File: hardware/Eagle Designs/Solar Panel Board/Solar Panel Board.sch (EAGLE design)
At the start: 34 parts, among them J1 MOLEX_503763-0291MOLEX_503763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, J2 MOLEX_503763-0491MOLEX_503763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

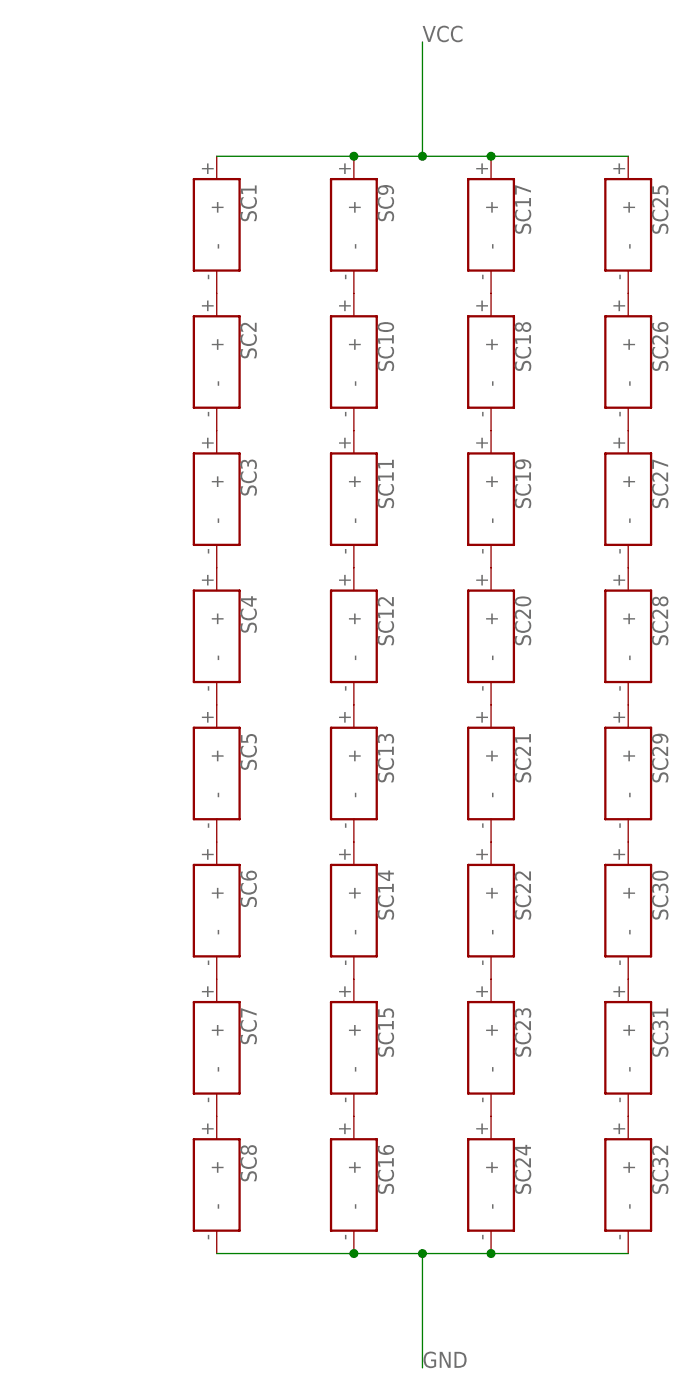
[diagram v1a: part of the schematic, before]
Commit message: Updated solar panel boards
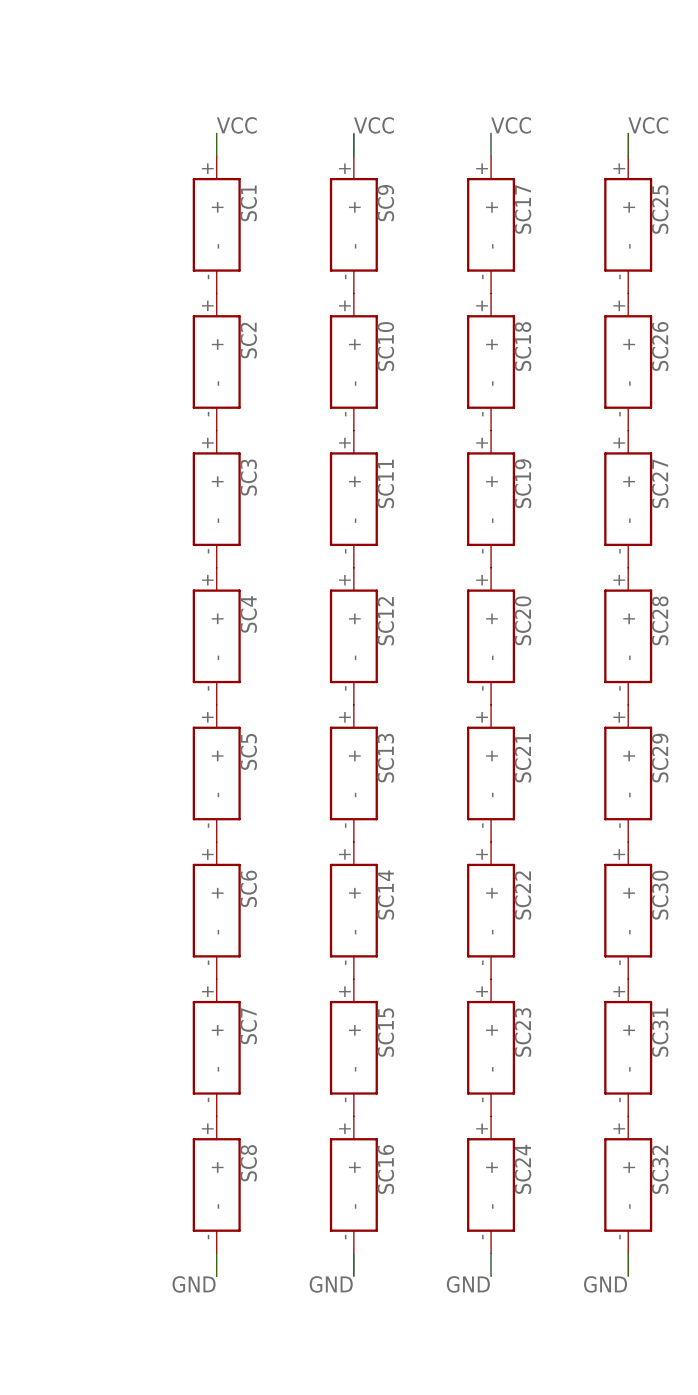
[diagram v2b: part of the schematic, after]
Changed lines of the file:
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@@
 </segment>
 <segment>
-<pinref part="J2" gate="G$0" pin="1"/>
+<pinref part="SC1" gate="G$1" pin="+"/>
+<wire x1="457.2" y1="43.18" x2="457.2" y2="45.72" width="0.1524" layer="91"/>
+<label x="457.2" y="45.72" size="1.778" layer="95"/>
+</segment>
+<segment>
+<pinref part="SC9" gate="G$1" pin="+"/>
+<wire x1="472.44" y1="43.18" x2="472.44" y2="45.72" width="0.1524" layer="91"/>
+<label x="472.44" y="45.72" size="1.778" layer="95"/>
+</segment>
+<segment>
+<pinref part="SC17" gate="G$1" pin="+"/>
+<wire x1="487.68" y1="43.18" x2="487.68" y2="45.72" width="0.1524" layer="91"/>
+<label x="487.68" y="45.72" size="1.778" layer="95"/>
+</segment>
+<segment>
+<pinref part="SC25" gate="G$1" pin="+"/>
+<wire x1="502.92" y1="43.18" x2="502.92" y2="45.72" width="0.1524" layer="91"/>
+<label x="502.92" y="45.72" size="1.778" layer="95"/>
+</segment>
+<segment>
 <wire x1="416.56" y1="-33.02" x2="419.1" y2="-33.02" width="0.1524" layer="91"/>
 <label x="419.1" y="-33.02" size="1.778" layer="95"/>
-</segment>
-<segment>
-<pinref part="SC25" gate="G$1" pin="+"/>
-<pinref part="SC17" gate="G$1" pin="+"/>
-<wire x1="487.68" y1="43.18" x2="502.92" y2="43.18" width="0.1524" layer="91"/>
-<junction x="487.68" y="43.18"/>
-<wire x1="480.06" y1="43.18" x2="487.68" y2="43.18" width="0.1524" layer="91"/>
-<wire x1="480.06" y1="43.18" x2="480.06" y2="55.88" width="0.1524" layer="91"/>
-<junction x="480.06" y="43.18"/>
-<pinref part="SC9" gate="G$1" pin="+"/>
-<pinref part="SC1" gate="G$1" pin="+"/>
-<wire x1="457.2" y1="43.18" x2="472.44" y2="43.18" width="0.1524" layer="91"/>
-<wire x1="472.44" y1="43.18" x2="480.06" y2="43.18" width="0.1524" layer="91"/>
-<junction x="472.44" y="43.18"/>
-<label x="480.06" y="55.88" size="1.778" layer="95"/>
-</segment>
-<segment>
-<pinref part="J2" gate="G$0" pin="2"/>
+<pinref part="J2" gate="G$0" pin="1"/>
+</segment>
+<segment>
 <wire x1="416.56" y1="-38.1" x2="419.1" y2="-38.1" width="0.1524" layer="91"/>
 <label x="419.1" y="-38.1" size="1.778" layer="95"/>
+<pinref part="J2" gate="G$0" pin="2"/>
 </segment>
 </net>
@@
 <net name="GND" class="0">
 <segment>
-<pinref part="J2" gate="G$0" pin="4"/>
+<pinref part="SC8" gate="G$1" pin="-"/>
+<wire x1="457.2" y1="-78.74" x2="457.2" y2="-81.28" width="0.1524" layer="91"/>
+<label x="457.2" y="-81.28" size="1.778" layer="95" rot="R180"/>
+</segment>
+<segment>
+<pinref part="SC16" gate="G$1" pin="-"/>
+<wire x1="472.44" y1="-78.74" x2="472.44" y2="-81.28" width="0.1524" layer="91"/>
+<label x="472.44" y="-81.28" size="1.778" layer="95" rot="R180"/>
+</segment>
+<segment>
+<pinref part="SC24" gate="G$1" pin="-"/>
+<wire x1="487.68" y1="-78.74" x2="487.68" y2="-81.28" width="0.1524" layer="91"/>
+<label x="487.68" y="-81.28" size="1.778" layer="95" rot="R180"/>
+</segment>
+<segment>
+<pinref part="SC32" gate="G$1" pin="-"/>
+<wire x1="502.92" y1="-78.74" x2="502.92" y2="-81.28" width="0.1524" layer="91"/>
+<label x="502.92" y="-81.28" size="1.778" layer="95" rot="R180"/>
+</segment>
+<segment>
+<wire x1="416.56" y1="2.54" x2="419.1" y2="2.54" width="0.1524" layer="91"/>
+<label x="419.1" y="2.54" size="1.778" layer="95"/>
+<pinref part="J1" gate="G$0" pin="MNT_1"/>
+</segment>
+<segment>
 <wire x1="416.56" y1="-48.26" x2="419.1" y2="-48.26" width="0.1524" layer="91"/>
 <label x="419.1" y="-48.26" size="1.778" layer="95"/>
-</segment>
-<segment>
-<pinref part="J1" gate="G$0" pin="MNT_1"/>
-<wire x1="416.56" y1="2.54" x2="419.1" y2="2.54" width="0.1524" layer="91"/>
-<label x="419.1" y="2.54" size="1.778" layer="95"/>
-</segment>
-<segment>
-<pinref part="J1" gate="G$0" pin="MNT_2"/>
+<pinref part="J2" gate="G$0" pin="4"/>
+</segment>
+<segment>
+<wire x1="416.56" y1="-58.42" x2="419.1" y2="-58.42" width="0.1524" layer="91"/>
+<label x="419.1" y="-58.42" size="1.778" layer="95"/>
+<pinref part="J2" gate="G$0" pin="MNT_2"/>
+</segment>
+<segment>
+<wire x1="416.56" y1="-53.34" x2="419.1" y2="-53.34" width="0.1524" layer="91"/>
+<label x="419.1" y="-53.34" size="1.778" layer="95"/>
+<pinref part="J2" gate="G$0" pin="MNT_1"/>
+</segment>
+<segment>
+<wire x1="416.56" y1="-43.18" x2="419.1" y2="-43.18" width="0.1524" layer="91"/>
+<label x="419.1" y="-43.18" size="1.778" layer="95"/>
+<pinref part="J2" gate="G$0" pin="3"/>
+</segment>
+<segment>
 <wire x1="416.56" y1="-2.54" x2="419.1" y2="-2.54" width="0.1524" layer="91"/>
 <label x="419.1" y="-2.54" size="1.778" layer="95"/>
-</segment>
-<segment>
-<pinref part="SC32" gate="G$1" pin="-"/>
-<pinref part="SC24" gate="G$1" pin="-"/>
-<wire x1="487.68" y1="-78.74" x2="502.92" y2="-78.74" width="0.1524" layer="91"/>
-<junction x="487.68" y="-78.74"/>
-<wire x1="480.06" y1="-78.74" x2="487.68" y2="-78.74" width="0.1524" layer="91"/>
-<wire x1="480.06" y1="-78.74" x2="480.06" y2="-91.44" width="0.1524" layer="91"/>
-<junction x="480.06" y="-78.74"/>
-<pinref part="SC16" gate="G$1" pin="-"/>
-<junction x="472.44" y="-78.74"/>
-<wire x1="472.44" y1="-78.74" x2="480.06" y2="-78.74" width="0.1524" layer="91"/>
-<pinref part="SC8" gate="G$1" pin="-"/>
-<wire x1="457.2" y1="-78.74" x2="472.44" y2="-78.74" width="0.1524" layer="91"/>
-<label x="480.06" y="-91.44" size="1.778" layer="95"/>
-</segment>
-<segment>
-<pinref part="J2" gate="G$0" pin="MNT_2"/>
-<wire x1="416.56" y1="-58.42" x2="419.1" y2="-58.42" width="0.1524" layer="91"/>
-<label x="419.1" y="-58.42" size="1.778" layer="95"/>
-</segment>
-<segment>
-<pinref part="J2" gate="G$0" pin="MNT_1"/>
-<wire x1="416.56" y1="-53.34" x2="419.1" y2="-53.34" width="0.1524" layer="91"/>
-<label x="419.1" y="-53.34" size="1.778" layer="95"/>
-</segment>
-<segment>
-<pinref part="J2" gate="G$0" pin="3"/>
-<wire x1="416.56" y1="-43.18" x2="419.1" y2="-43.18" width="0.1524" layer="91"/>
-<label x="419.1" y="-43.18" size="1.778" layer="95"/>
-</segment>
-</net>
+<pinref part="J1" gate="G$0" pin="MNT_2"/>
+</segment>
+</net>

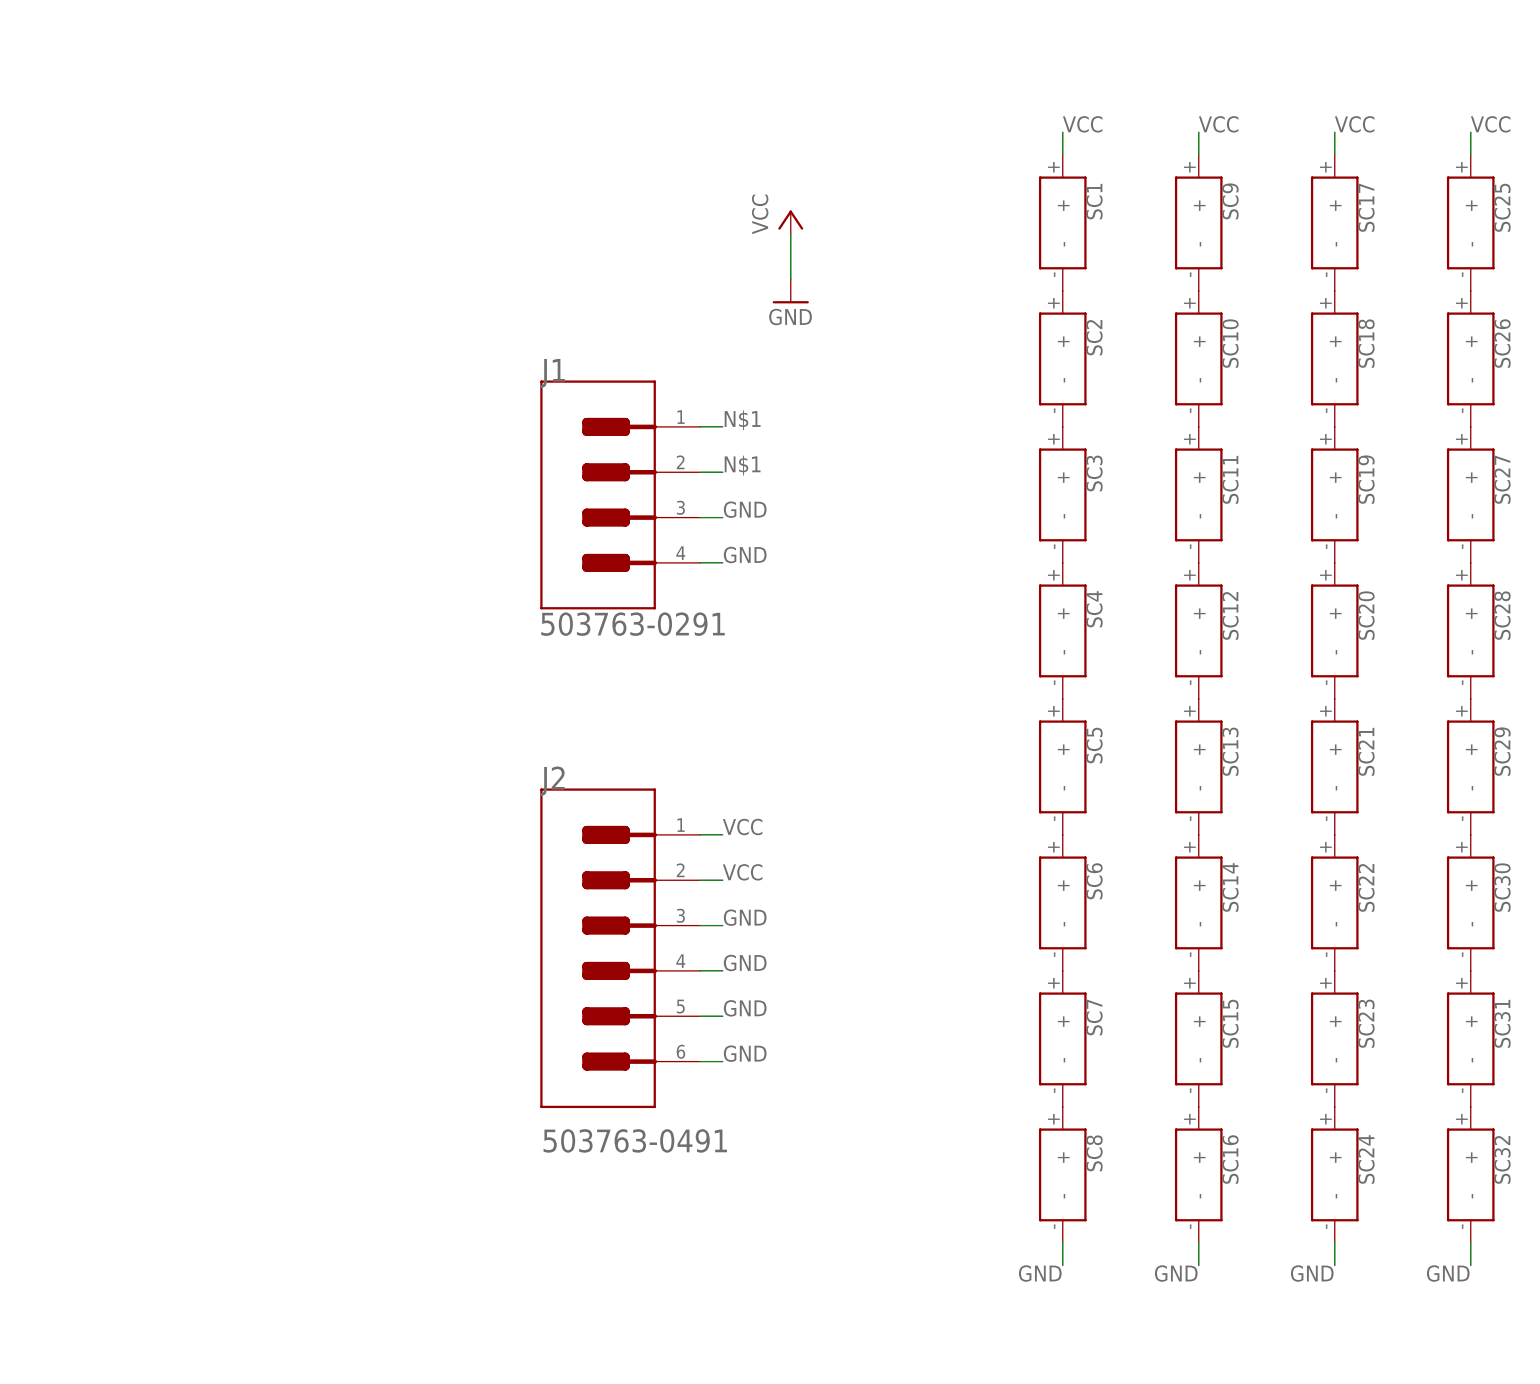
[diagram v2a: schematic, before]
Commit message: Solar panel board changes
Added temp sensor and external connector to solar panel board; updated solar panel board BOM
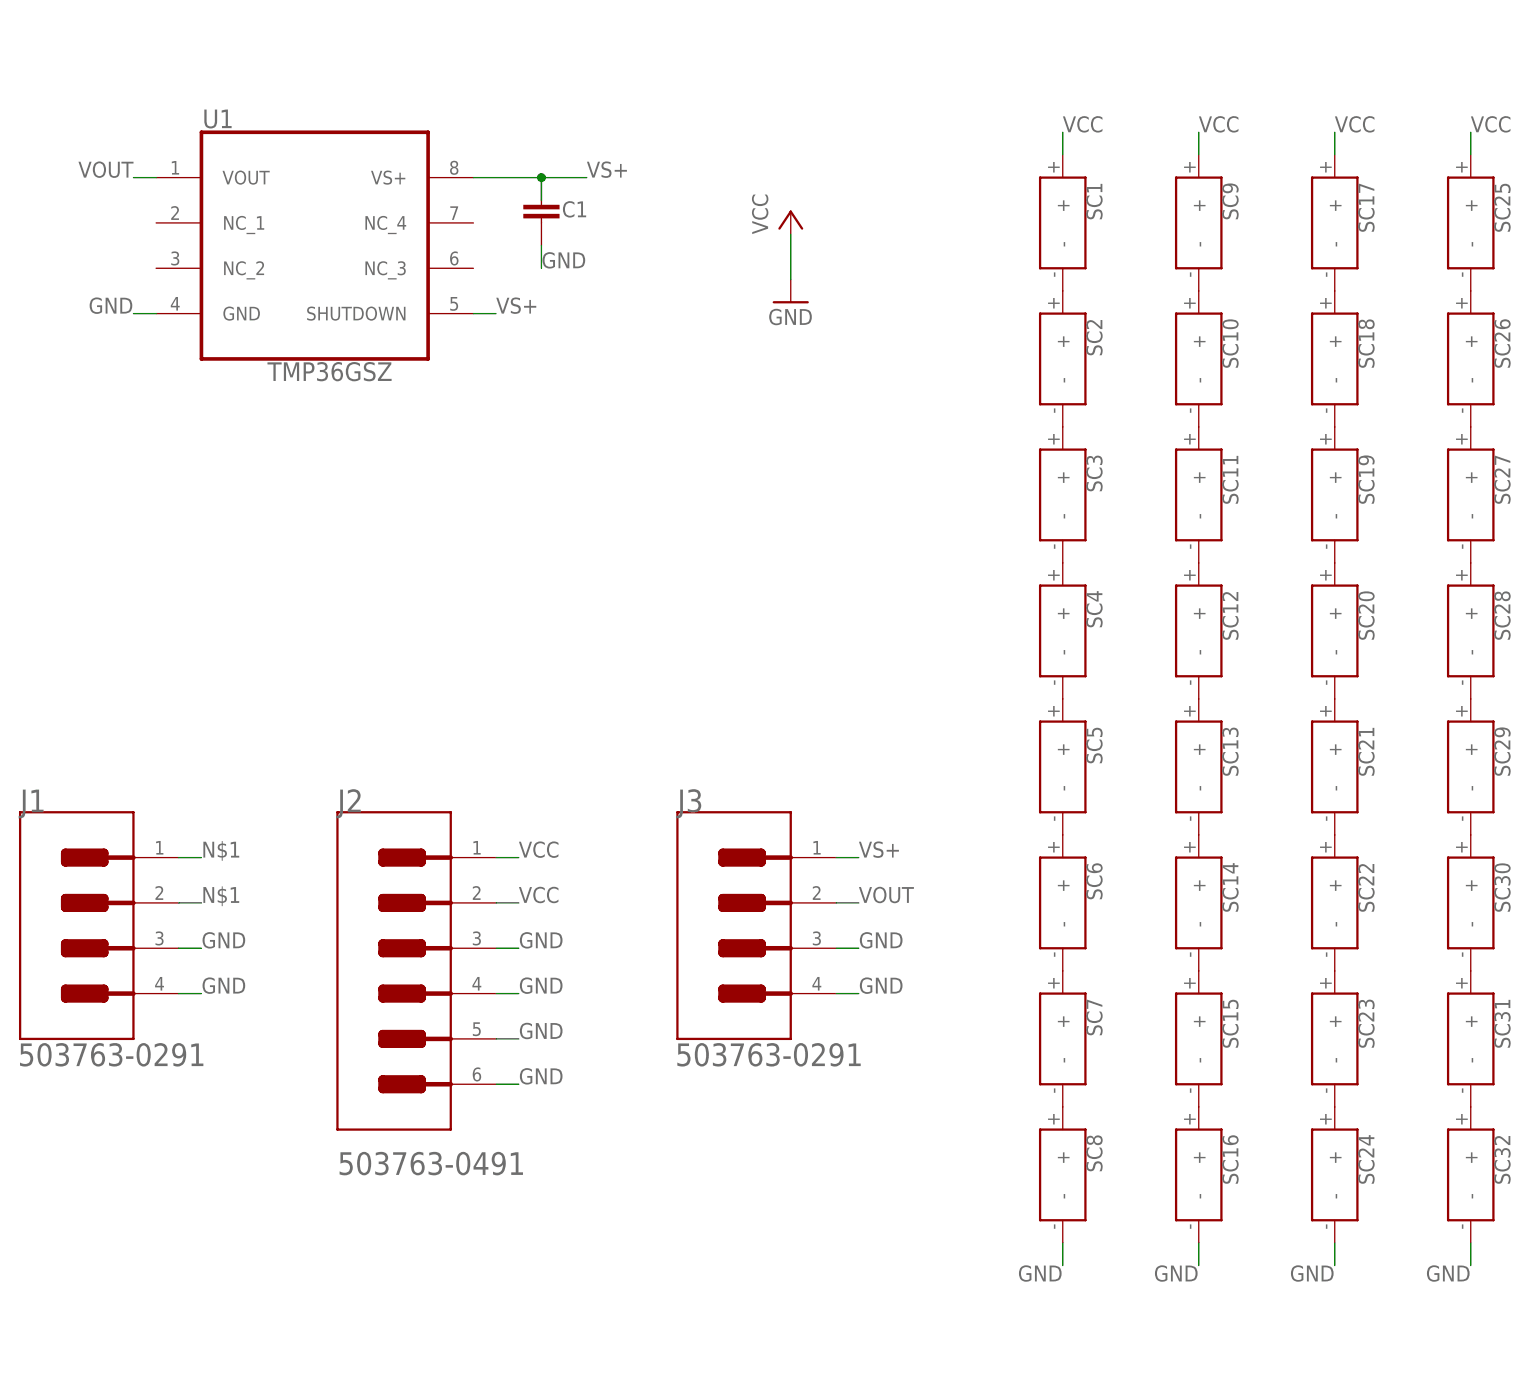
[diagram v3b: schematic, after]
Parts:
- added C1: (no value), HSFL_Main_Library:CAP0805
- added J3: MOLEX_503763-0291MOLEX_503763-0291_0_0, Molex - 503763-0291:MOLEX_503763-0291MOLEX_503763-0291_0_0
- added U1: TMP36GSZ, TMP36GSZ:TMP36GSZ
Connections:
- new net VOUT: J3.2, U1.VOUT
- new net VS+: C1.1, J3.1, U1.SHUTDOWN, U1.VS+
- net GND: now also C1.2, J3.MNT_1, J3.MNT_2, U1.GND
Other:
- moved on the sheet: J1, J2

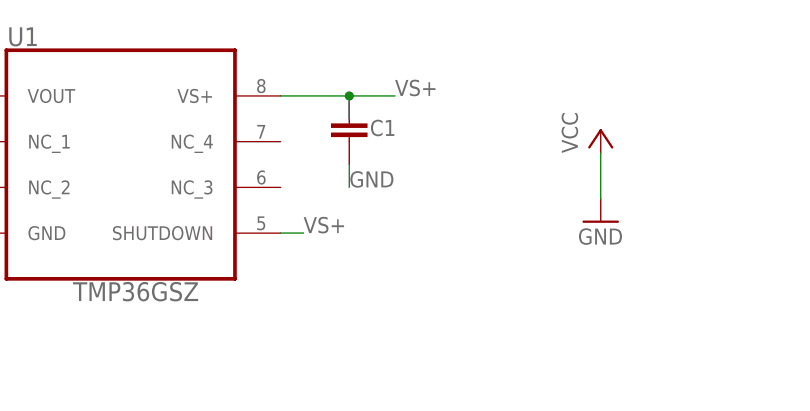
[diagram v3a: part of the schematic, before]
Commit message: Added values to resistors and capacitors
Payload - added 3.3k value to pullup resistors for H-bridges
Solar Panel Board - added 0.1uF value to capacitor for temp sensor
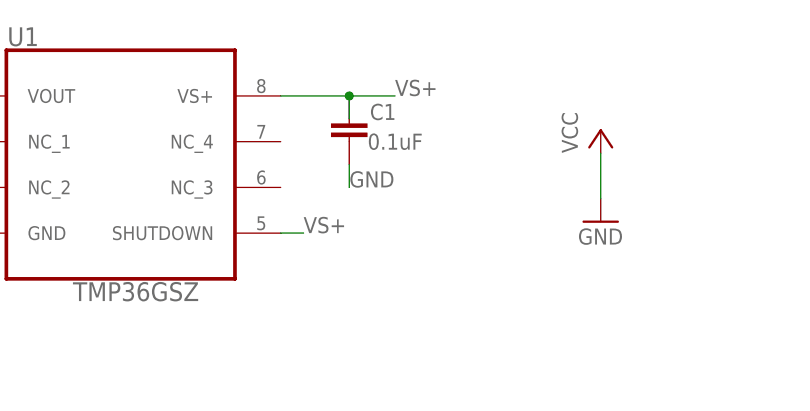
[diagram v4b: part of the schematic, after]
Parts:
- C1: value (none) -> 0.1uF
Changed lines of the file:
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@@
 <part name="U1" library="TMP36GSZ" deviceset="TMP36GSZ" device=""/>
 <part name="J3" library="Molex - 503763-0291" deviceset="MOLEX_503763-0291" device="MOLEX_503763-0291_0_0"/>
-<part name="C1" library="HSFL_Main_Library" deviceset="CAP" device="0805"/>
+<part name="C1" library="HSFL_Main_Library" deviceset="CAP" device="0805" value="0.1uF"/>
 </parts>
 <sheets>
@@
 </instance>
 <instance part="C1" gate="G$1" x="398.78" y="35.56" smashed="yes">
-<attribute name="NAME" x="401.066" y="36.195" size="1.778" layer="95"/>
-<attribute name="VALUE" x="400.304" y="33.401" size="1.778" layer="96"/>
+<attribute name="NAME" x="401.066" y="37.973" size="1.778" layer="95"/>
+<attribute name="VALUE" x="400.812" y="34.671" size="1.778" layer="96"/>
 </instance>
 </instances>
